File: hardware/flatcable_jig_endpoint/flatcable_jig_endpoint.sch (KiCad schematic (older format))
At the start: 2 parts

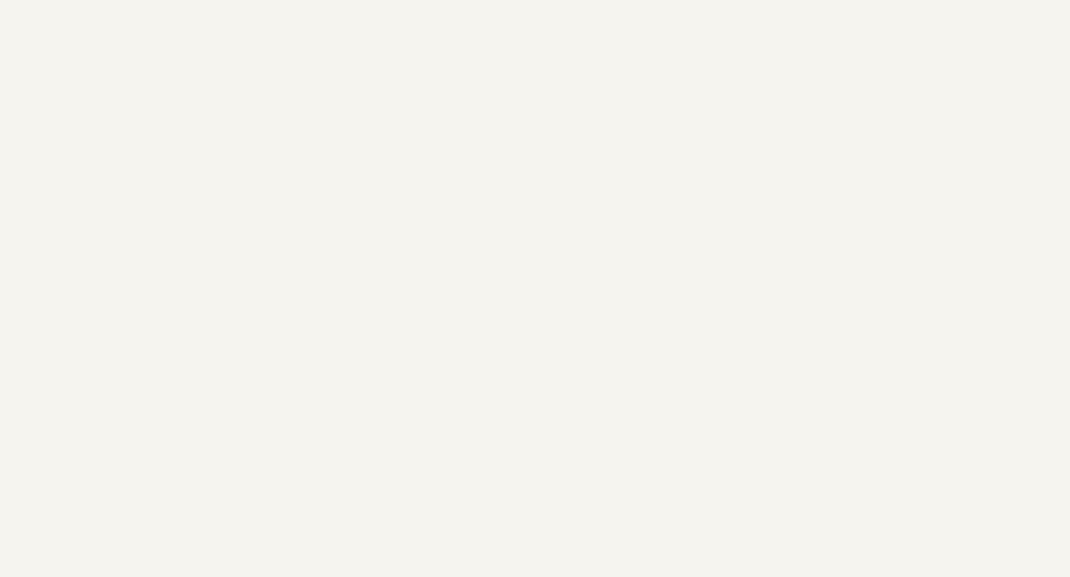
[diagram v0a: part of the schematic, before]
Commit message: updated schematic with a few parts
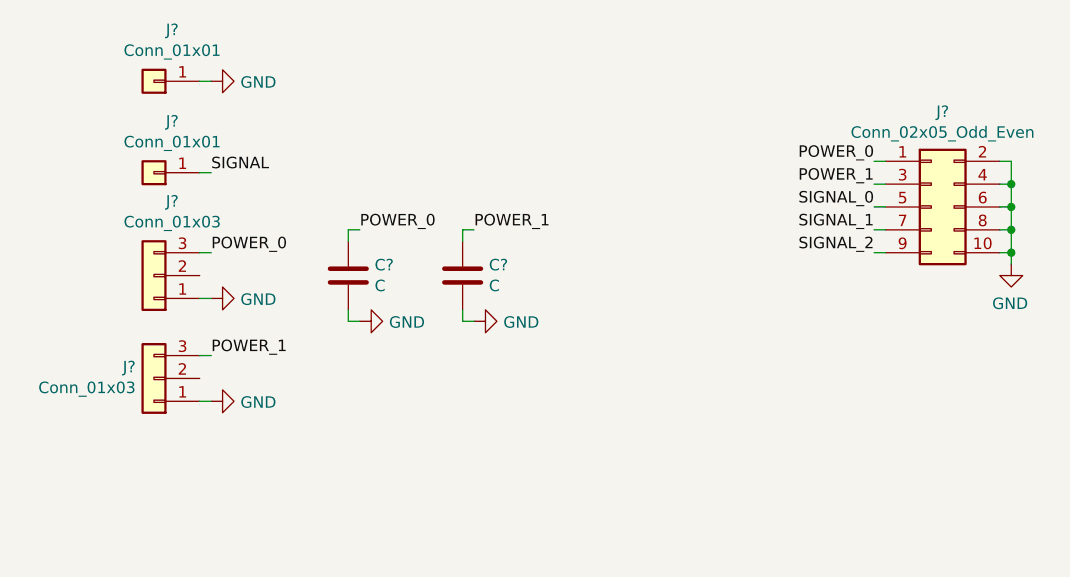
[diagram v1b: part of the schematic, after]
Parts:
- added C? (x2): C, SquantorRcl:C_0805, symbol Device:C
- added J? (x2): Conn_01x01, symbol Connector_Generic:Conn_01x01
- added J? (x2): Conn_01x03, symbol Connector_Generic:Conn_01x03
- added J?: Conn_02x05_Odd_Even, symbol Connector_Generic:Conn_02x05_Odd_Even
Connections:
- new net GND: C?.2, C?.2, J?.1 (Pin_1), J?.1 (Pin_1), J?.1 (Pin_1), J?.10 (Pin_10), J?.2 (Pin_2), J?.4 (Pin_4), J?.6 (Pin_6), J?.8 (Pin_8)
- new net POWER_0: C?.1, J?.1 (Pin_1), J?.3 (Pin_3)
- new net POWER_1: C?.1, J?.3 (Pin_3), J?.3 (Pin_3)
- new net SIGNAL: J?.1 (Pin_1)
- new net SIGNAL_0: J?.5 (Pin_5)
- new net SIGNAL_1: J?.7 (Pin_7)
- new net SIGNAL_2: J?.9 (Pin_9)
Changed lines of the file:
@@
 EESchema Schematic File Version 4
-LIBS:OSH_Park_2_layer-cache
 EELAYER 26 0
 EELAYER END
@@
 	1    0    0    -1
 $EndComp
+$Comp
+L Connector_Generic:Conn_01x01 J?
+U 1 1 5C14DC59
+P 950 1350
+F 0 "J?" H 870 1125 50  0000 C CNN
+F 1 "Conn_01x01" H 870 1216 50  0000 C CNN
+F 2 "" H 950 1350 50  0001 C CNN
+F 3 "~" H 950 1350 50  0001 C CNN
+	1    950  1350
+	-1   0    0    1
+$EndComp
+$Comp
+L Connector_Generic:Conn_01x01 J?
+U 1 1 5C14DD34
+P 950 1750
+F 0 "J?" H 870 1525 50  0000 C CNN
+F 1 "Conn_01x01" H 870 1616 50  0000 C CNN
+F 2 "" H 950 1750 50  0001 C CNN
+F 3 "~" H 950 1750 50  0001 C CNN
+	1    950  1750
+	-1   0    0    1
+$EndComp
+$Comp
+L power:GND #PWR?
+U 1 1 5C14DD89
+P 1200 1350
+F 0 "#PWR?" H 1200 1100 50  0001 C CNN
+F 1 "GND" V 1205 1222 50  0000 R CNN
+F 2 "" H 1200 1350 50  0001 C CNN
+F 3 "" H 1200 1350 50  0001 C CNN
+	1    1200 1350
+	0    -1   1    0
+$EndComp
+Wire Wire Line
+	1150 1350 1200 1350
+$Comp
+L Connector_Generic:Conn_01x03 J?
+U 1 1 5C14DEA6
+P 950 2200
+F 0 "J?" H 870 1875 50  0000 C CNN
+F 1 "Conn_01x03" H 870 1966 50  0000 C CNN
+F 2 "" H 950 2200 50  0001 C CNN
+F 3 "~" H 950 2200 50  0001 C CNN
+	1    950  2200
+	-1   0    0    1
+$EndComp
+$Comp
+L Connector_Generic:Conn_01x03 J?
+U 1 1 5C14DF05
+P 950 2650
+F 0 "J?" H 1030 2600 50  0000 L CNN
+F 1 "Conn_01x03" H 1030 2691 50  0000 L CNN
+F 2 "" H 950 2650 50  0001 C CNN
+F 3 "~" H 950 2650 50  0001 C CNN
+	1    950  2650
+	-1   0    0    1
+$EndComp
+$Comp
+L power:GND #PWR?
+U 1 1 5C14E194
+P 1200 2300
+F 0 "#PWR?" H 1200 2050 50  0001 C CNN
+F 1 "GND" V 1205 2172 50  0000 R CNN
+F 2 "" H 1200 2300 50  0001 C CNN
+F 3 "" H 1200 2300 50  0001 C CNN
+	1    1200 2300
+	0    -1   1    0
+$EndComp
+$Comp
+L power:GND #PWR?
+U 1 1 5C14E1AD
+P 1200 2750
+F 0 "#PWR?" H 1200 2500 50  0001 C CNN
+F 1 "GND" V 1205 2622 50  0000 R CNN
+F 2 "" H 1200 2750 50  0001 C CNN
+F 3 "" H 1200 2750 50  0001 C CNN
+	1    1200 2750
+	0    -1   1    0
+$EndComp
+Wire Wire Line
+	1150 2300 1200 2300
+Wire Wire Line
+	1200 2750 1150 2750
+$Comp
+L Connector_Generic:Conn_02x05_Odd_Even J?
+U 1 1 5C14E46A
+P 4350 1900
+F 0 "J?" H 4400 2317 50  0000 C CNN
+F 1 "Conn_02x05_Odd_Even" H 4400 2226 50  0000 C CNN
+F 2 "" H 4350 1900 50  0001 C CNN
+F 3 "~" H 4350 1900 50  0001 C CNN
+	1    4350 1900
+	1    0    0    -1
+$EndComp
+$Comp
+L power:GND #PWR?
+U 1 1 5C14E4F7
+P 4700 2150
+F 0 "#PWR?" H 4700 1900 50  0001 C CNN
+F 1 "GND" H 4705 1977 50  0000 C CNN
+F 2 "" H 4700 2150 50  0001 C CNN
+F 3 "" H 4700 2150 50  0001 C CNN
+	1    4700 2150
+	-1   0    0    -1
+$EndComp
+Wire Wire Line
+	4650 1700 4700 1700
+Wire Wire Line
+	4700 1700 4700 1800
+Wire Wire Line
+	4650 2100 4700 2100
+Connection ~ 4700 2100
+Wire Wire Line
+	4700 2100 4700 2150
+Wire Wire Line
+	4650 2000 4700 2000
+Connection ~ 4700 2000
+Wire Wire Line
+	4700 2000 4700 2100
+Wire Wire Line
+	4650 1900 4700 1900
+Connection ~ 4700 1900
+Wire Wire Line
+	4700 1900 4700 2000
+Wire Wire Line
+	4650 1800 4700 1800
+Connection ~ 4700 1800
+Wire Wire Line
+	4700 1800 4700 1900
+Wire Wire Line
+	4150 1700 4100 1700
+Wire Wire Line
+	4150 1800 4100 1800
+Wire Wire Line
+	4150 1900 4100 1900
+Wire Wire Line
+	4150 2000 4100 2000
+Wire Wire Line
+	4150 2100 4100 2100
+Text Label 4100 1900 2    50   ~ 0
+SIGNAL_0
+Text Label 4100 2000 2    50   ~ 0
+SIGNAL_1
+Text Label 4100 2100 2    50   ~ 0
+SIGNAL_2
+Text Label 4100 1700 2    50   ~ 0
+POWER_0
+Text Label 4100 1800 2    50   ~ 0
+POWER_1
+Wire Wire Line
+	1150 1750 1200 1750
+Text Label 1200 1750 0    50   ~ 0
+SIGNAL
+Text Label 1200 2100 0    50   ~ 0
+POWER_0
+Text Label 1200 2550 0    50   ~ 0
+POWER_1
+Wire Wire Line
+	1150 2100 1200 2100
+Wire Wire Line
+	1150 2550 1200 2550
+$Comp
+L Device:C C?
+U 1 1 5C14F5BC
+P 1800 2200
+F 0 "C?" H 1915 2246 50  0000 L CNN
+F 1 "C" H 1915 2155 50  0000 L CNN
+F 2 "SquantorRcl:C_0805" H 1838 2050 50  0001 C CNN
+F 3 "~" H 1800 2200 50  0001 C CNN
+	1    1800 2200
+	1    0    0    -1
+$EndComp
+$Comp
+L Device:C C?
+U 1 1 5C14F6B5
+P 2300 2200
+F 0 "C?" H 2415 2246 50  0000 L CNN
+F 1 "C" H 2415 2155 50  0000 L CNN
+F 2 "SquantorRcl:C_0805" H 2338 2050 50  0001 C CNN
+F 3 "~" H 2300 2200 50  0001 C CNN
+	1    2300 2200
+	1    0    0    -1
+$EndComp
+Text Label 1850 2000 0    50   ~ 0
+POWER_0
+$Comp
+L power:GND #PWR?
+U 1 1 5C14F709
+P 1850 2400
+F 0 "#PWR?" H 1850 2150 50  0001 C CNN
+F 1 "GND" V 1855 2272 50  0000 R CNN
+F 2 "" H 1850 2400 50  0001 C CNN
+F 3 "" H 1850 2400 50  0001 C CNN
+	1    1850 2400
+	0    -1   1    0
+$EndComp
+$Comp
+L power:GND #PWR?
+U 1 1 5C14F726
+P 2350 2400
+F 0 "#PWR?" H 2350 2150 50  0001 C CNN
+F 1 "GND" V 2355 2272 50  0000 R CNN
+F 2 "" H 2350 2400 50  0001 C CNN
+F 3 "" H 2350 2400 50  0001 C CNN
+	1    2350 2400
+	0    -1   1    0
+$EndComp
+Wire Wire Line
+	1850 2400 1800 2400
+Wire Wire Line
+	1800 2400 1800 2350
+Wire Wire Line
+	2300 2350 2300 2400
+Wire Wire Line
+	2300 2400 2350 2400
+Text Label 2350 2000 0    50   ~ 0
+POWER_1
+Wire Wire Line
+	1800 2050 1800 2000
+Wire Wire Line
+	1800 2000 1850 2000
+Wire Wire Line
+	2300 2050 2300 2000
+Wire Wire Line
+	2300 2000 2350 2000
 $EndSCHEMATC

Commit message: started layout, still need to add the endpad connections
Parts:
- added R1, R2, R3, R4, R5, R6, R7, R8, R9: R, SquantorRcl:R_0603_hand, symbol Device:R
- J3, J4: renamed from J?; footprint (none) -> Connector_Molex:Molex_KK-254_AE-6410-03A_1x03_P2.54mm_Vertical
- J5: renamed from J?; footprint (none) -> SquantorConnectors:Header-0254-2X05-H010
- gave numbers to parts that had none: 4
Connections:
- net GND: now also R1.1, R2.1, R3.1, R7.1, R8.1, R9.1
- net SIGNAL: now also R1.2, R2.2, R3.2, R4.2, R5.2, R6.2
- net SIGNAL_0: now also R4.1, R7.2
- net SIGNAL_1: now also R5.1, R8.2
- net SIGNAL_2: now also R6.1, R9.2
- no-connect marks 0 -> 2
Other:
- moved on the sheet: J5

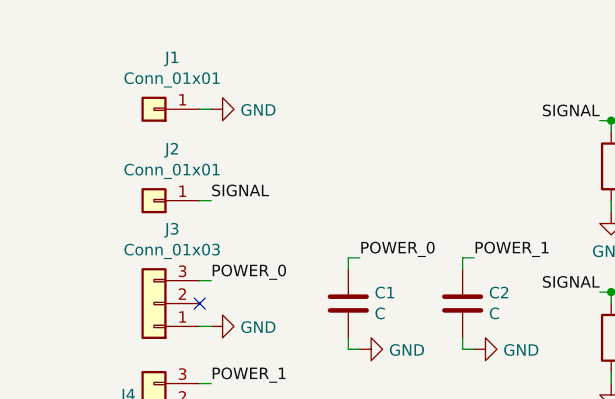
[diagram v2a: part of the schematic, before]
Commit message: layout completed, now silk screen
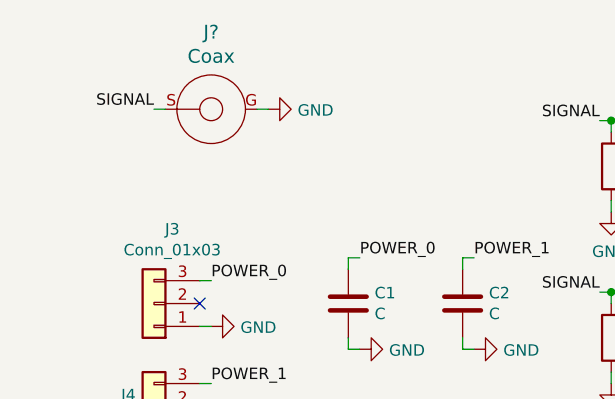
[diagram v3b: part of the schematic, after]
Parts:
- removed J1, J2: Conn_01x01, symbol Connector_Generic:Conn_01x01
- added J?: Coax, SquantorConnectors:Conn_BNC_RightAngle_TH, symbol SquantorConnectors:Coax
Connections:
- net GND: now also J?.G
- net SIGNAL: now also J?.S
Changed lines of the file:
@@
-$EndComp
-$Comp
-L Connector_Generic:Conn_01x01 J1
-U 1 1 5C14DC59
-P 950 1350
-F 0 "J1" H 870 1125 50  0000 C CNN
-F 1 "Conn_01x01" H 870 1216 50  0000 C CNN
-F 2 "" H 950 1350 50  0001 C CNN
-F 3 "~" H 950 1350 50  0001 C CNN
-	1    950  1350
-	-1   0    0    1
-$EndComp
-$Comp
-L Connector_Generic:Conn_01x01 J2
-U 1 1 5C14DD34
-P 950 1750
-F 0 "J2" H 870 1525 50  0000 C CNN
-F 1 "Conn_01x01" H 870 1616 50  0000 C CNN
-F 2 "" H 950 1750 50  0001 C CNN
-F 3 "~" H 950 1750 50  0001 C CNN
-	1    950  1750
-	-1   0    0    1
 $EndComp
 $Comp
 L power:GND #PWR0101
 U 1 1 5C14DD89
-P 1200 1350
-F 0 "#PWR0101" H 1200 1100 50  0001 C CNN
-F 1 "GND" V 1205 1222 50  0000 R CNN
-F 2 "" H 1200 1350 50  0001 C CNN
-F 3 "" H 1200 1350 50  0001 C CNN
-	1    1200 1350
+P 1450 1350
+F 0 "#PWR0101" H 1450 1100 50  0001 C CNN
+F 1 "GND" V 1455 1222 50  0000 R CNN
+F 2 "" H 1450 1350 50  0001 C CNN
+F 3 "" H 1450 1350 50  0001 C CNN
+	1    1450 1350
 	0    -1   1    0
 $EndComp
-Wire Wire Line
-	1150 1350 1200 1350
 $Comp
 L Connector_Generic:Conn_01x03 J3
@@
 Text Label 4850 1800 2    50   ~ 0
 POWER_1
-Wire Wire Line
-	1150 1750 1200 1750
-Text Label 1200 1750 0    50   ~ 0
+Text Label 950  1350 2    50   ~ 0
 SIGNAL
 Text Label 1200 2100 0    50   ~ 0
@@
 	3400 2950 3350 2950
 Connection ~ 3350 2950
+$Comp
+L SquantorConnectors:Coax J?
+U 1 1 5C16C2B5
+P 1200 1350
+F 0 "J?" H 1200 1687 60  0000 C CNN
+F 1 "Coax" H 1200 1581 60  0000 C CNN
+F 2 "SquantorConnectors:Conn_BNC_RightAngle_TH" H 1200 1350 60  0001 C CNN
+F 3 "" H 1200 1350 60  0001 C CNN
+	1    1200 1350
+	1    0    0    -1
+$EndComp
+Wire Wire Line
+	950  1350 1000 1350
+Wire Wire Line
+	1400 1350 1450 1350
 $EndSCHEMATC

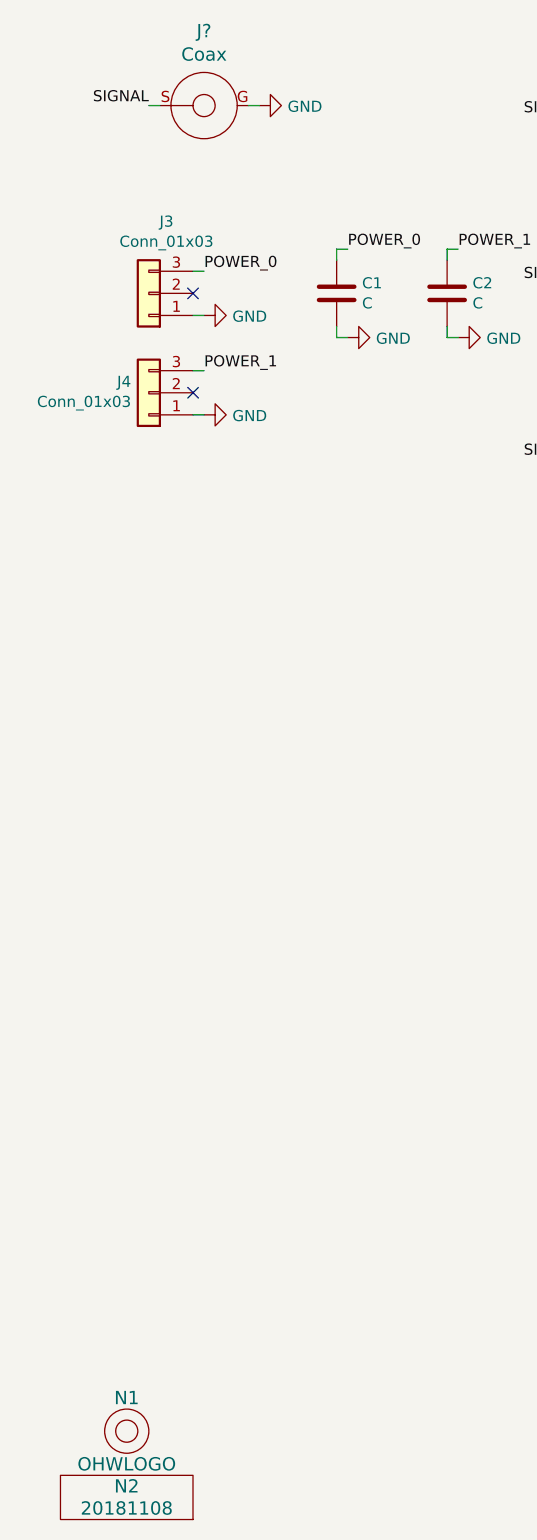
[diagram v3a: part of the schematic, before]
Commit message: updated versionnumber, adjusted cutout line thickness to 0.1mm
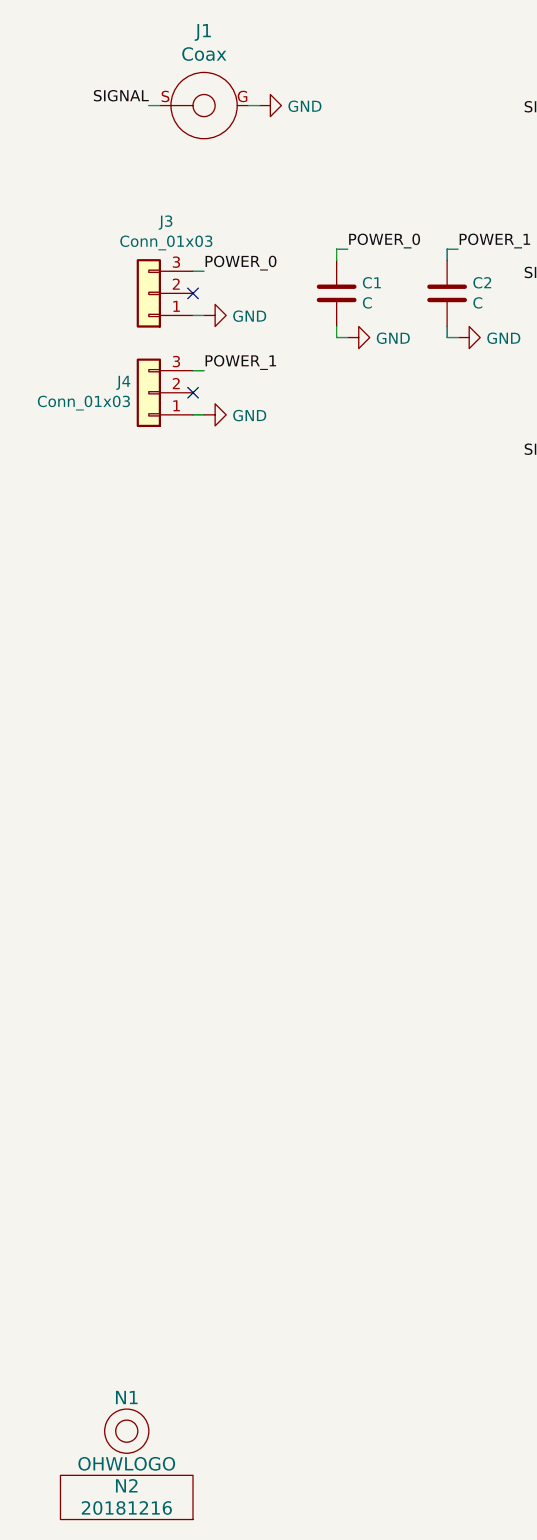
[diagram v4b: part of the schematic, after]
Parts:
- N2: value 20181108 -> 20181216
- gave numbers to parts that had none: 1
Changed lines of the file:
@@
 EESchema Schematic File Version 4
+LIBS:flatcable_jig_endpoint-cache
 EELAYER 26 0
 EELAYER END
@@
 P 850 7700
 F 0 "N2" H 850 7800 60  0000 C CNN
-F 1 "20181108" H 850 7700 60  0000 C CNN
+F 1 "20181216" H 850 7700 60  0000 C CNN
 F 2 "SquantorLabels:Label_version" H 850 7700 60  0001 C CNN
 F 3 "" H 850 7700 60  0001 C CNN
@@
 Connection ~ 3350 2950
 $Comp
-L SquantorConnectors:Coax J?
+L SquantorConnectors:Coax J1
 U 1 1 5C16C2B5
 P 1200 1350
-F 0 "J?" H 1200 1687 60  0000 C CNN
+F 0 "J1" H 1200 1687 60  0000 C CNN
 F 1 "Coax" H 1200 1581 60  0000 C CNN
 F 2 "SquantorConnectors:Conn_BNC_RightAngle_TH" H 1200 1350 60  0001 C CNN
